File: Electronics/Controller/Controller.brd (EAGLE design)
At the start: 190 x 90 mm, 16 parts, among them Q1 BS250, U1 GY-521MPU6050, X1 Battery

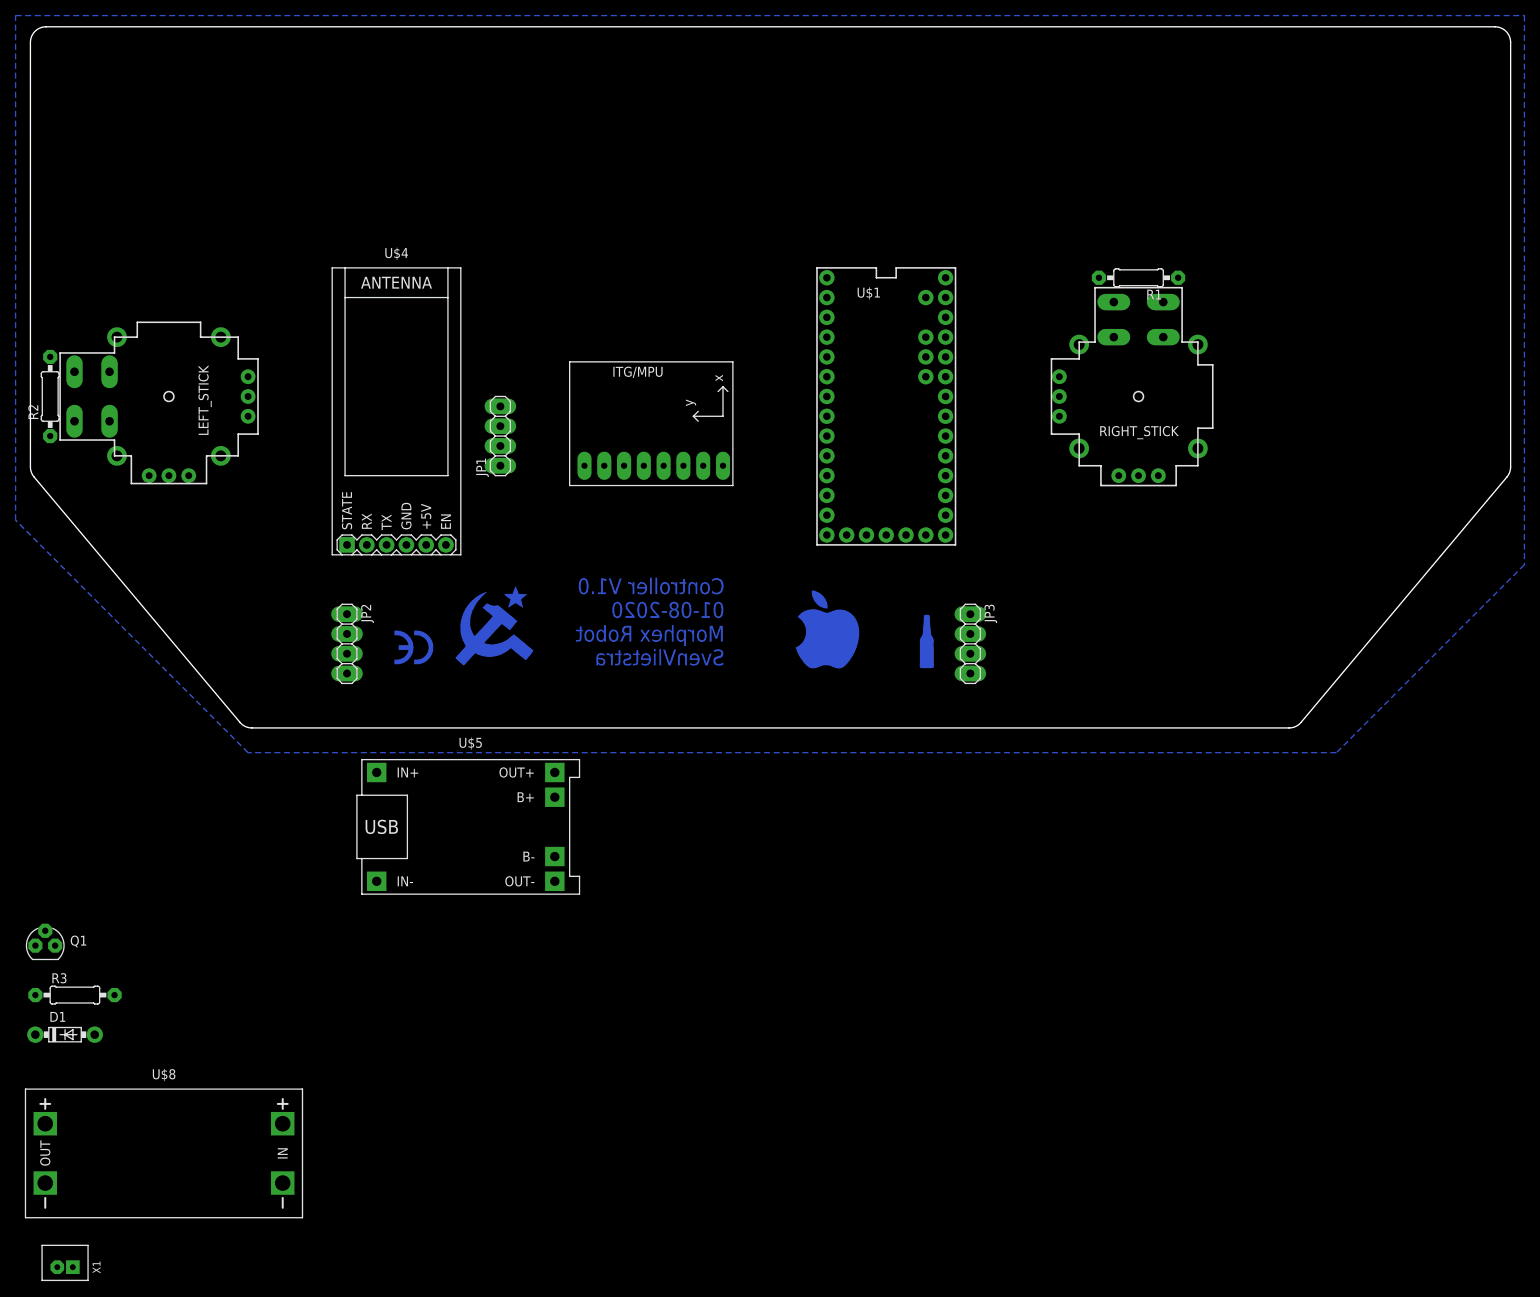
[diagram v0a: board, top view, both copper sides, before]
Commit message: Automatic source change
Added automatic source change and fixing librabry's for better overview
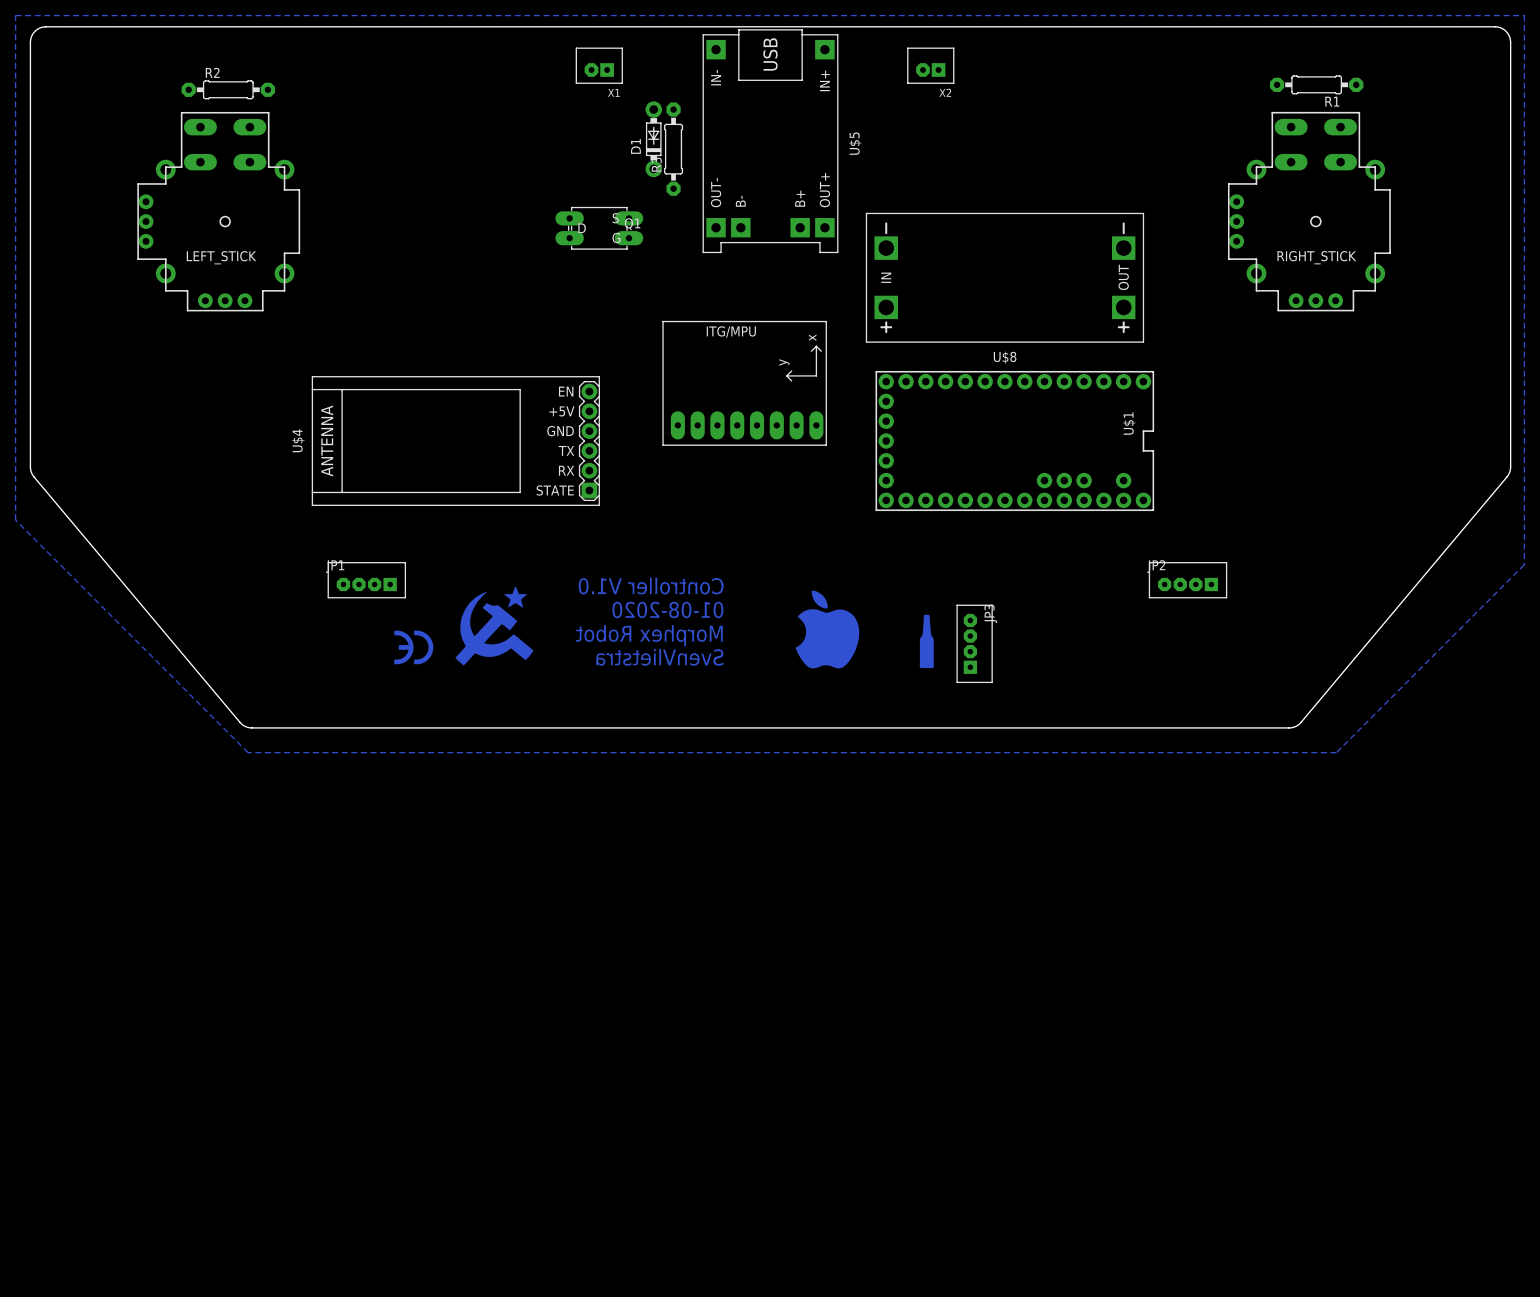
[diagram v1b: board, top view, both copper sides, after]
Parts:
- added X2: Switch, con-JST PH:B2B-PH-K-S
- JP1, JP2, JP3: value (none) -> B4B-PH-K-S; device pinhead:1X04 -> con-JST PH:B4B-PH-K-S
- Q1: value BS250 -> IRFD9014; device transistor-small-signal:SOT54E -> transistor-small-signal:C370-01
- moved X1 168.3 mm to (73.0, 84.5)
- moved U$8 155.8 mm to (125.1, 57.8), turned to 180 degrees
- moved D1 137.6 mm to (80.0, 75.6), turned to 90 degrees
- moved R3 133.0 mm to (82.5, 74.3), turned to 90 degrees
- moved Q1 116.3 mm to (73.0, 64.1)
- moved JP2 108.2 mm to (148.6, 18.4), turned to 0 degrees
- moved U$5 95.8 mm to (95.0, 75.0), turned to 270 degrees
- moved R2 45.5 mm to (25.4, 81.9), turned to 0 degrees
- moved R1 33.7 mm to (165.1, 82.5)
- moved RIGHT_STICK 32.0 mm to (165.0, 65.0)
- moved JP1 25.6 mm to (43.2, 18.4), turned to 0 degrees
- moved LEFT_STICK 23.6 mm to (25.0, 65.0), turned to 0 degrees
- moved U$1 17.1 mm to (126.4, 36.8), turned to 270 degrees
- moved U1 13.1 mm to (92.0, 47.7)
- moved U$4 8.52 mm to (54.6, 36.8), turned to 90 degrees
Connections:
- new net N$6: U$8.OUT+, X2.2
- net N$4: now also Q1.D1, X2.1; no longer U$8.OUT+

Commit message: Buzzer, Teensy 4.0 Robot
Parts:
- added R4: 2K2, rcl:0207/10
- added SG1: F/EE17P, buzzer:F/EE17P
- added T1: (no value), transistor:TO92-EBC
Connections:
- new net BUZZER: R4.1, U$1.4
- new net N$7: R4.2, T1.B
- new net N$8: SG1.2, T1.C
- net +5V: now also SG1.1
- net GND: now also T1.E
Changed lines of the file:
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@@
 <?xml version="1.0" encoding="utf-8"?>
 <!DOCTYPE eagle SYSTEM "eagle.dtd">
-<eagle version="9.6.2">
+<eagle version="9.6.1">
 <drawing>
 <settings>
@@
 <layer number="115" name="ReferenceISLANDS" color="7" fill="1" visible="no" active="yes"/>
 <layer number="116" name="centerDrill" color="9" fill="1" visible="no" active="yes"/>
+<layer number="117" name="BOX" color="8" fill="0" visible="yes" active="yes"/>
 <layer number="118" name="Rect_Pads" color="7" fill="1" visible="no" active="yes"/>
 <layer number="121" name="_tsilk" color="7" fill="1" visible="no" active="yes"/>
@@
 </layers>
 <board>
-<fusionsync huburn="a.cGVyc29uYWw6dWUyOTc0MmJh" projecturn="a.cGVyc29uYWw6dWUyOTc0MmJhIzIwMTgxMjAxMTYzMjc3MDgx" f3durn="urn:adsk.wipprod:dm.lineage:tMrdlwCdQ7a2oWCIA8Xtng" pcbguid="" lastpulledtime="2020-08-01T14:53:25Z" lastsyncedchangeguid="" latestrevisionid="8c6db879-796b-4f26-8c43-a56c9cbb9a75" lastsyncedrevisionid="60fe7847-9d48-48c6-a7f4-c77f49cd8f4f" lastboardhashguid="a3af47ca-199c-871d-6a89-2919f351b28c" lastpushedtime="2020-04-27T18:36:54Z" linktopcb3d="true"/>
+<fusionsync huburn="a.cGVyc29uYWw6dWUyOTc0MmJh" projecturn="a.cGVyc29uYWw6dWUyOTc0MmJhIzIwMTgxMjAxMTYzMjc3MDgx" f3durn="urn:adsk.wipprod:dm.lineage:tMrdlwCdQ7a2oWCIA8Xtng" pcbguid="" lastpulledtime="2020-08-01T14:53:25Z" lastsyncedchangeguid="" latestrevisionid="8c6db879-796b-4f26-8c43-a56c9cbb9a75" lastsyncedrevisionid="60fe7847-9d48-48c6-a7f4-c77f49cd8f4f" lastboardhashguid="a3af47ca-199c-871d-6a89-2919f351b28c" lastpushedtime="2020-04-27T18:36:54Z" linktopcb3d="%12"/>
 <plain>
 <text x="89.11413125" y="8.03174375" size="2.032" layer="16" font="vector" ratio="21" rot="MR0">Controller V1.0
@@
 <attribute name="VALUE" x="117.84" y="88.265" size="1.016" layer="27" align="bottom-right"/>
 </element>
+<element name="SG1" library="buzzer" library_urn="urn:adsk.eagle:library:113" package="F/EE17P" package3d_urn="urn:adsk.eagle:package:5285/1" value="F/EE17P" x="166.37" y="29.21" smashed="yes">
+<attribute name="MF" value="" x="166.37" y="29.21" size="1.778" layer="27" display="off"/>
+<attribute name="MPN" value="" x="166.37" y="29.21" size="1.778" layer="27" display="off"/>
+<attribute name="NAME" x="170.815" y="36.83" size="1.27" layer="25" ratio="10"/>
+<attribute name="OC_FARNELL" value="unknown" x="166.37" y="29.21" size="1.778" layer="27" display="off"/>
+<attribute name="OC_NEWARK" value="unknown" x="166.37" y="29.21" size="1.778" layer="27" display="off"/>
+<attribute name="POPULARITY" value="0" x="166.37" y="29.21" size="1.778" layer="27" display="off"/>
+<attribute name="VALUE" x="162.56" y="24.13" size="1.27" layer="27" ratio="10"/>
+</element>
+<element name="T1" library="transistor" library_urn="urn:adsk.eagle:library:402" package="TO92-EBC" package3d_urn="urn:adsk.eagle:package:29915/2" value="" x="177.165" y="40.005" smashed="yes" rot="R270">
+<attribute name="NAME" x="178.943" y="42.545" size="1.27" layer="25" ratio="10" rot="R270"/>
+<attribute name="POPULARITY" value="0" x="177.165" y="40.005" size="1.778" layer="27" rot="R270" display="off"/>
+<attribute name="VALUE" x="172.593" y="42.545" size="1.27" layer="27" ratio="10" rot="R270"/>
+</element>
+<element name="R4" library="rcl" library_urn="urn:adsk.eagle:library:334" package="0207/10" package3d_urn="urn:adsk.eagle:package:23491/2" value="2K2" x="166.37" y="40.005" smashed="yes">
+<attribute name="NAME" x="163.322" y="41.529" size="1.27" layer="25" ratio="10"/>
+<attribute name="POPULARITY" value="81" x="166.37" y="40.005" size="1.778" layer="27" display="off"/>
+<attribute name="SPICEPREFIX" value="R" x="166.37" y="40.005" size="1.778" layer="27" display="off"/>
+<attribute name="VALUE" x="164.1094" y="39.37" size="1.27" layer="27" ratio="10"/>
+</element>
 </elements>
 <signals>
@@
 <contactref element="U$5" pad="IN-"/>
 <contactref element="U$8" pad="IN-"/>
+<contactref element="T1" pad="E"/>
 <wire x1="172.6161" y1="71.6704" x2="170.18" y2="82.55" width="0" layer="19" extent="1-1"/>
 <wire x1="172.6161" y1="58.3354" x2="172.6161" y2="71.6704" width="0" layer="19" extent="1-1"/>
@@
 <wire x1="20.32" y1="81.915" x2="17.3785" y2="71.6658" width="0" layer="19" extent="1-1"/>
 <wire x1="32.6185" y1="71.6658" x2="32.6185" y2="58.3308" width="0" layer="19" extent="1-1"/>
+<wire x1="175.895" y1="42.545" x2="40.18" y2="18.415" width="0" layer="19" extent="1-1"/>
 </signal>
 <signal name="X-AXIS1">
@@
 <contactref element="R3" pad="2"/>
 <contactref element="U$8" pad="IN+"/>
+<contactref element="SG1" pad="1"/>
 <wire x1="82.55" y1="79.375" x2="101.9802" y2="87.0674" width="0" layer="19" extent="1-1"/>
 <wire x1="80.01" y1="79.375" x2="82.55" y2="79.375" width="0" layer="19" extent="1-1"/>
@@
 <wire x1="109.855" y1="53.975" x2="101.9802" y2="87.0674" width="0" layer="19" extent="1-1"/>
 <wire x1="142.8682" y1="29.2125" x2="109.855" y2="53.975" width="0" layer="19" extent="1-1"/>
+<wire x1="161.3662" y1="29.21" x2="46.18" y2="18.415" width="0" layer="19" extent="1-1"/>
 </signal>
 <signal name="26/A12/DAC">
@@
 <wire x1="140.335" y1="53.975" x2="114.57" y2="84.455" width="0" layer="19" extent="1-1"/>
 </signal>
+<signal name="N$7">
+<contactref element="R4" pad="2"/>
+<contactref element="T1" pad="B"/>
+<wire x1="175.895" y1="40.005" x2="171.45" y2="40.005" width="0" layer="19" extent="1-1"/>
+</signal>
+<signal name="N$8">
+<contactref element="T1" pad="C"/>
+<contactref element="SG1" pad="2"/>
+<wire x1="171.3738" y1="29.21" x2="175.895" y2="37.465" width="0" layer="19" extent="1-1"/>
+</signal>
+<signal name="BUZZER">
+<contactref element="R4" pad="1"/>
+<contactref element="U$1" pad="4"/>
+<wire x1="130.1682" y1="44.4525" x2="161.29" y2="40.005" width="0" layer="19" extent="1-1"/>
+</signal>
 </signals>

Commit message: .....
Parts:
- removed JP1, JP2, JP3: B4B-PH-K-S, con-JST PH:B4B-PH-K-S
- added BUT_L, BUT_R, NEXTION: B4B-PH-K-S, con-JST PH:B4B-PH-K-S
- moved T1 137.4 mm to (40.0, 48.3)
- moved SG1 129.6 mm to (36.8, 34.3)
- moved R4 119.0 mm to (47.6, 48.3), turned to 180 degrees
- moved U$4 70.0 mm to (124.5, 41.3), turned to 270 degrees
- moved U$1 57.0 mm to (69.8, 44.4), turned to 0 degrees
- moved X1 33.3 mm to (95.2, 59.7), flipped to the bottom, turned to 180 degrees
- moved U$8 17.1 mm to (113.7, 70.5), turned to 90 degrees
- moved X2 12.1 mm to (127.6, 85.7), turned to 180 degrees
- moved Q1 9.16 mm to (67.9, 71.8)
- moved U1 6.42 mm to (97.9, 45.2), turned to 0 degrees
- moved D1 4.58 mm to (77.5, 71.8)
- moved R3 4.58 mm to (80.0, 70.5)
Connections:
- net +3V3: now also BUT_L.1, BUT_L.3, BUT_R.1, BUT_R.3; no longer JP2.1, JP2.3, JP3.1, JP3.3
- net +5V: now also NEXTION.1; no longer JP1.1
- net BUT_1: now also BUT_L.2, U$1.22/A8; no longer JP2.2, U$1.20/A6
- net BUT_2: now also BUT_L.4, U$1.23/A9; no longer JP2.4, U$1.21/A7
- net BUT_3: now also BUT_R.2, U$1.20/A6; no longer JP3.2, U$1.22/A8
- net BUT_4: now also BUT_R.4, U$1.21/A7; no longer JP3.4, U$1.23/A9
- net GND: now also NEXTION.4; no longer JP1.4
- net NEX_RX: now also NEXTION.2; no longer JP1.2
- net NEX_TX: now also NEXTION.3; no longer JP1.3
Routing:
- net +3V3: track 0.00 -> 109.2 mm
- net BL_TX: track 0.00 -> 101.5 mm
- net BL_RX: track 0.00 -> 87.7 mm
- net BUT_2: track 0.00 -> 45.0 mm
- net BUT_1: track 0.00 -> 39.3 mm
- net +5V: track 0.00 -> 34.6 mm
- net BUT_4: track 0.00 -> 31.6 mm
- net SW1: track 0.00 -> 26.7 mm
- net BUT_3: track 0.00 -> 24.8 mm
- net GY_SDA: track 0.00 -> 13.9 mm
- net GY_SCL: track 0.00 -> 13.9 mm
- net N$8: track 0.00 -> 12.7 mm
- net BUZZER: track 0.00 -> 9.53 mm
- net NEX_RX: track 0.00 -> 8.37 mm
- net NEX_TX: track 0.00 -> 8.36 mm
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- added copper zone on layer 1, net GND
